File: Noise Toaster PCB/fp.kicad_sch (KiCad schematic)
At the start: 29 parts, among them J1 Line Out, SW1 Manual Gate, SW2 Repeat

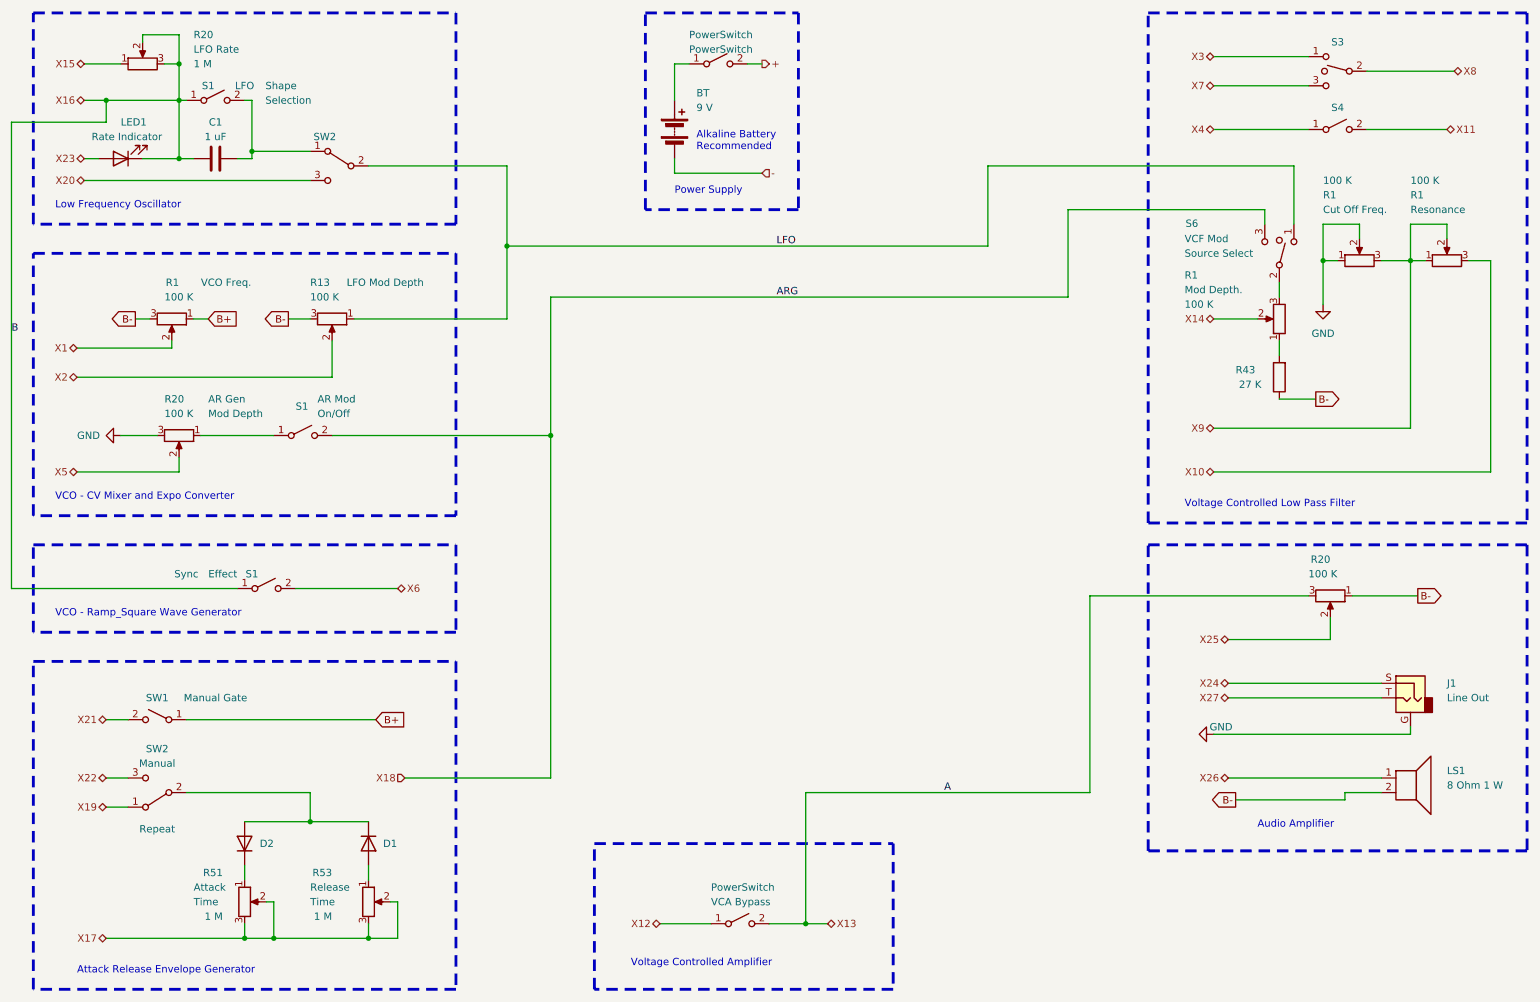
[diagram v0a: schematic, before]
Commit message: color coded wireing and added color legend
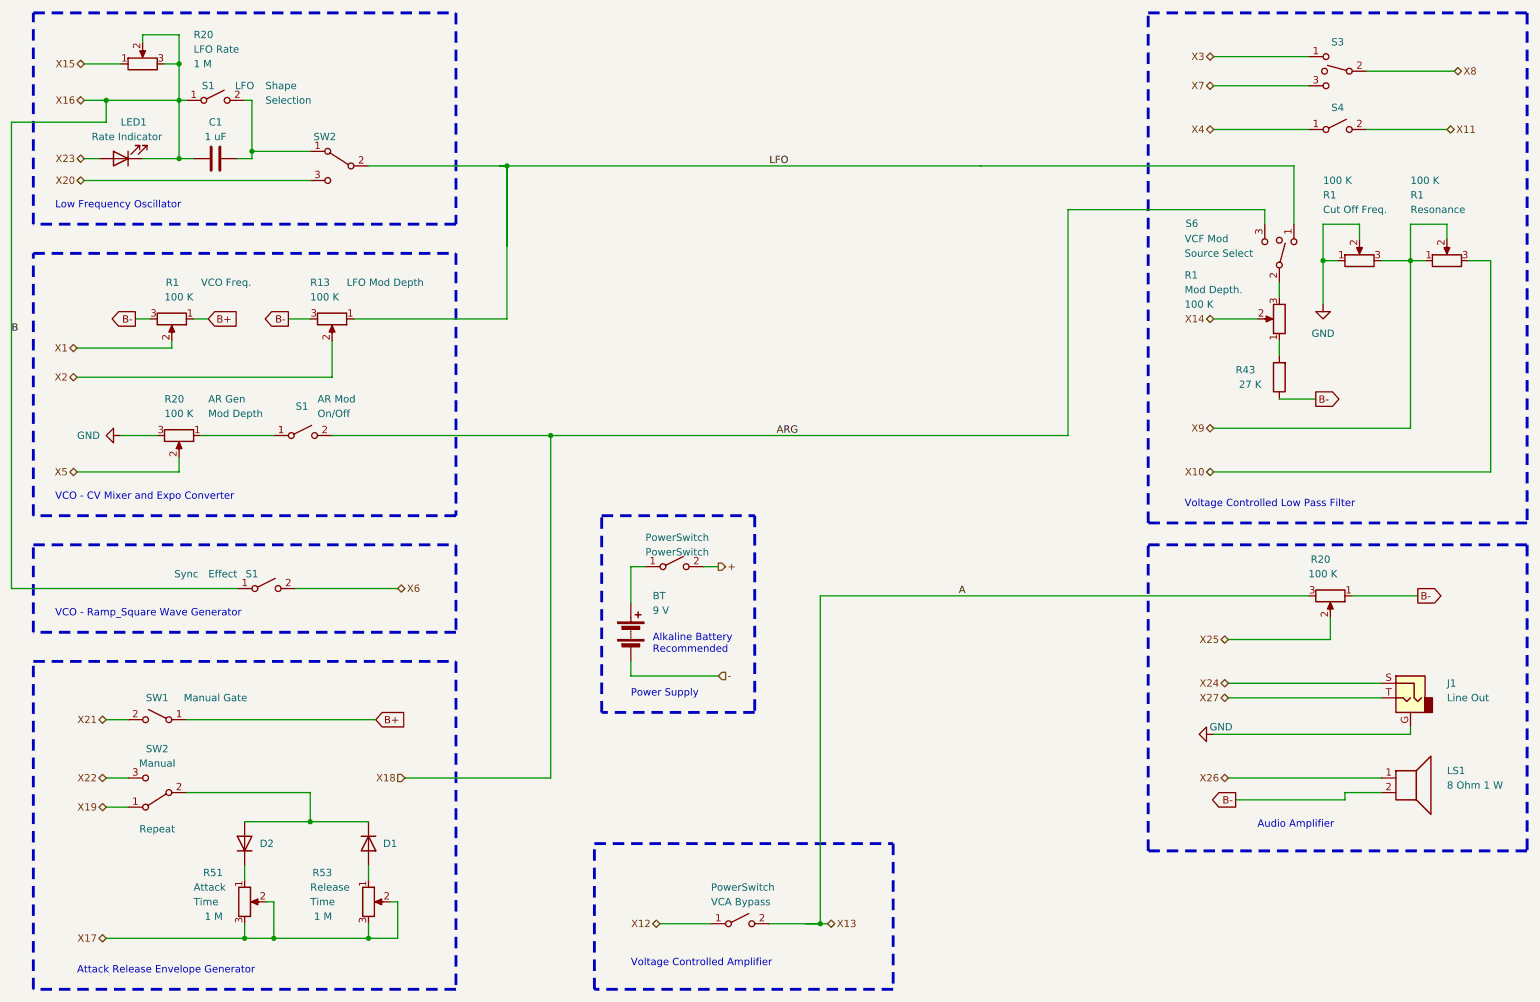
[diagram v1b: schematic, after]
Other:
- moved on the sheet: BT, PowerSwitch
